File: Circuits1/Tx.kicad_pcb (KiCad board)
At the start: 2 copper layers, 43.2 x 51.4 mm, 54 parts, among them CON1 USB-MINI-B, P1 CONN_3X2, SW1 SW_PUSH, SW2 Power Select, U1 ATMEGA32U4, U2 LD1117, U3 NRF24L01+, U4 MPU-6050, X1 QUARTZ, X2 QUARTZ

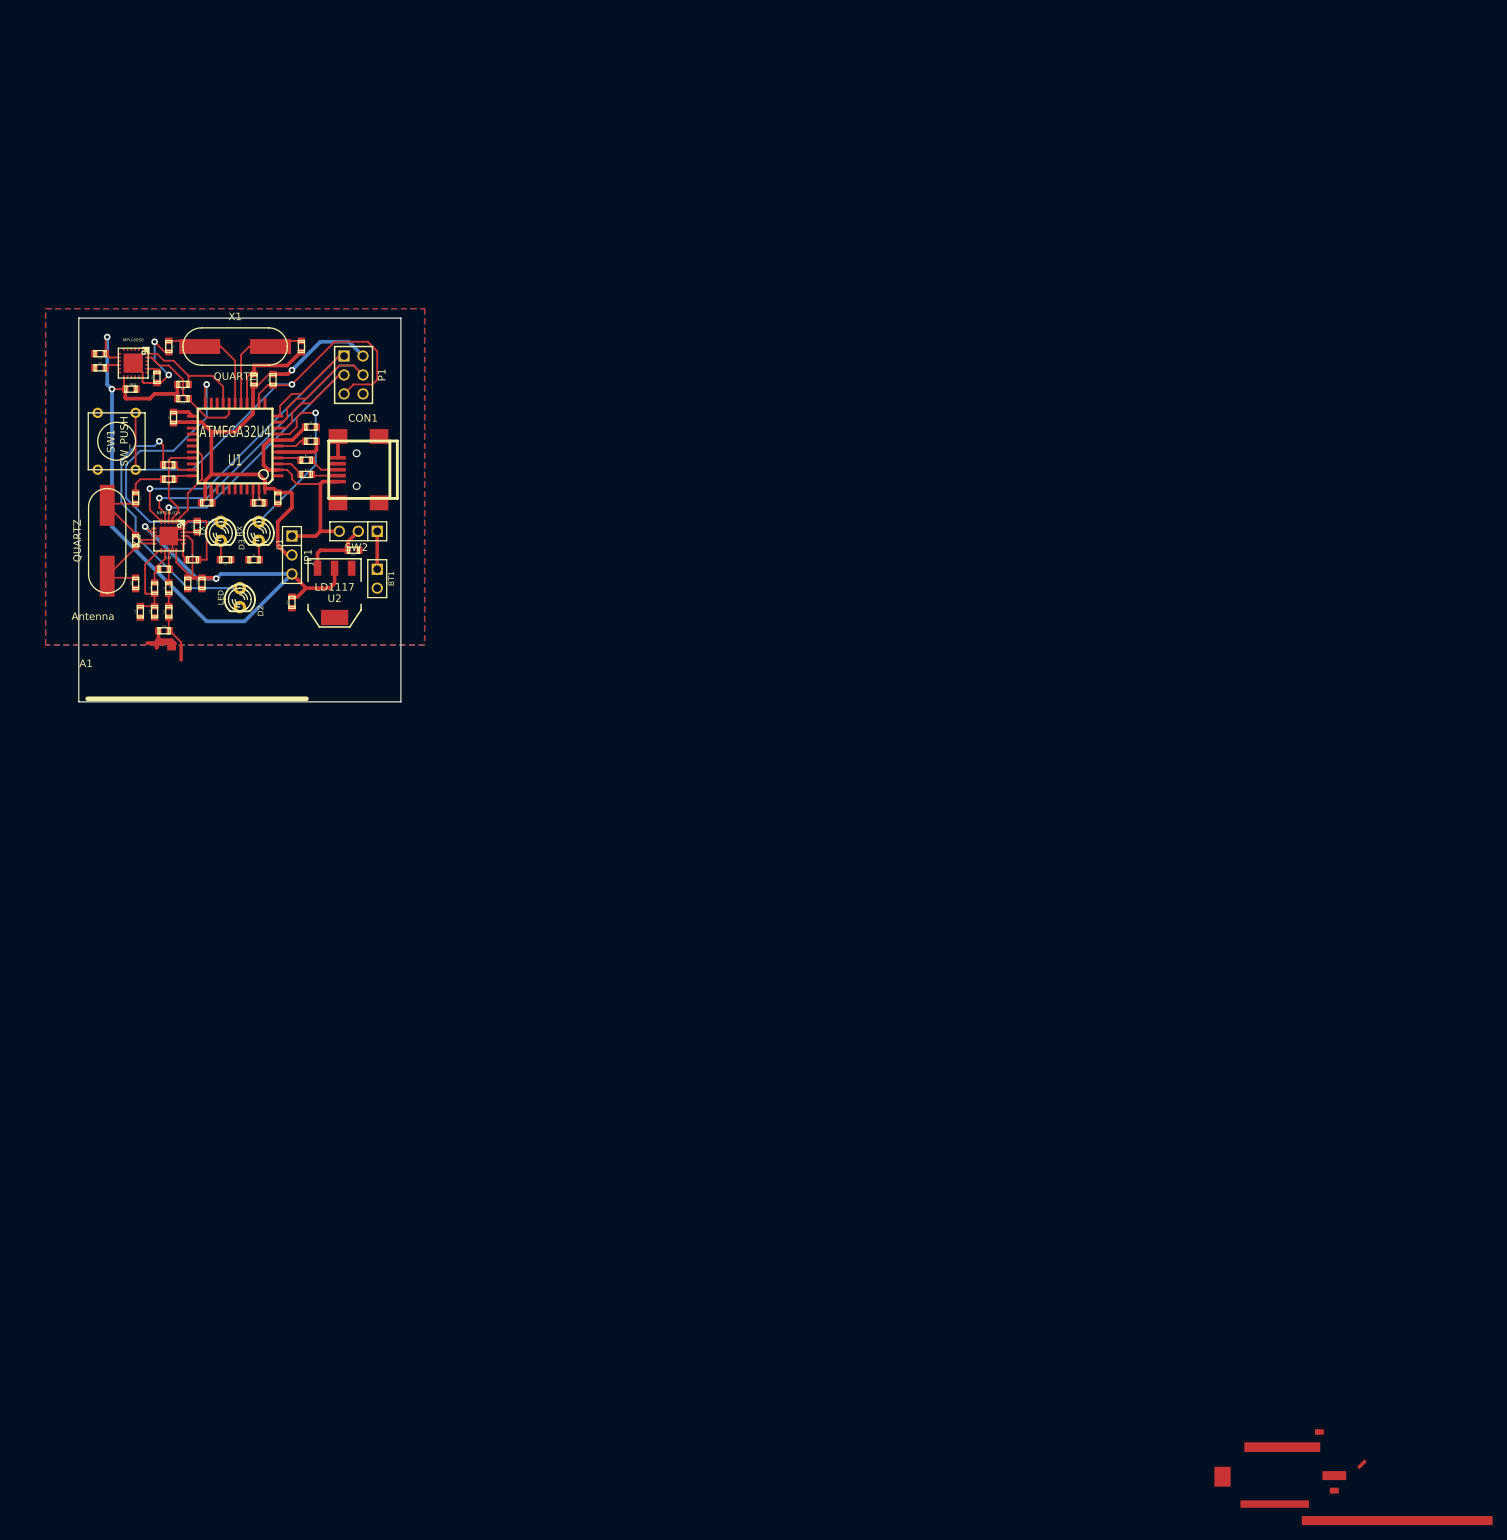
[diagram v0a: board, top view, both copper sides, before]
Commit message: Antenna Position
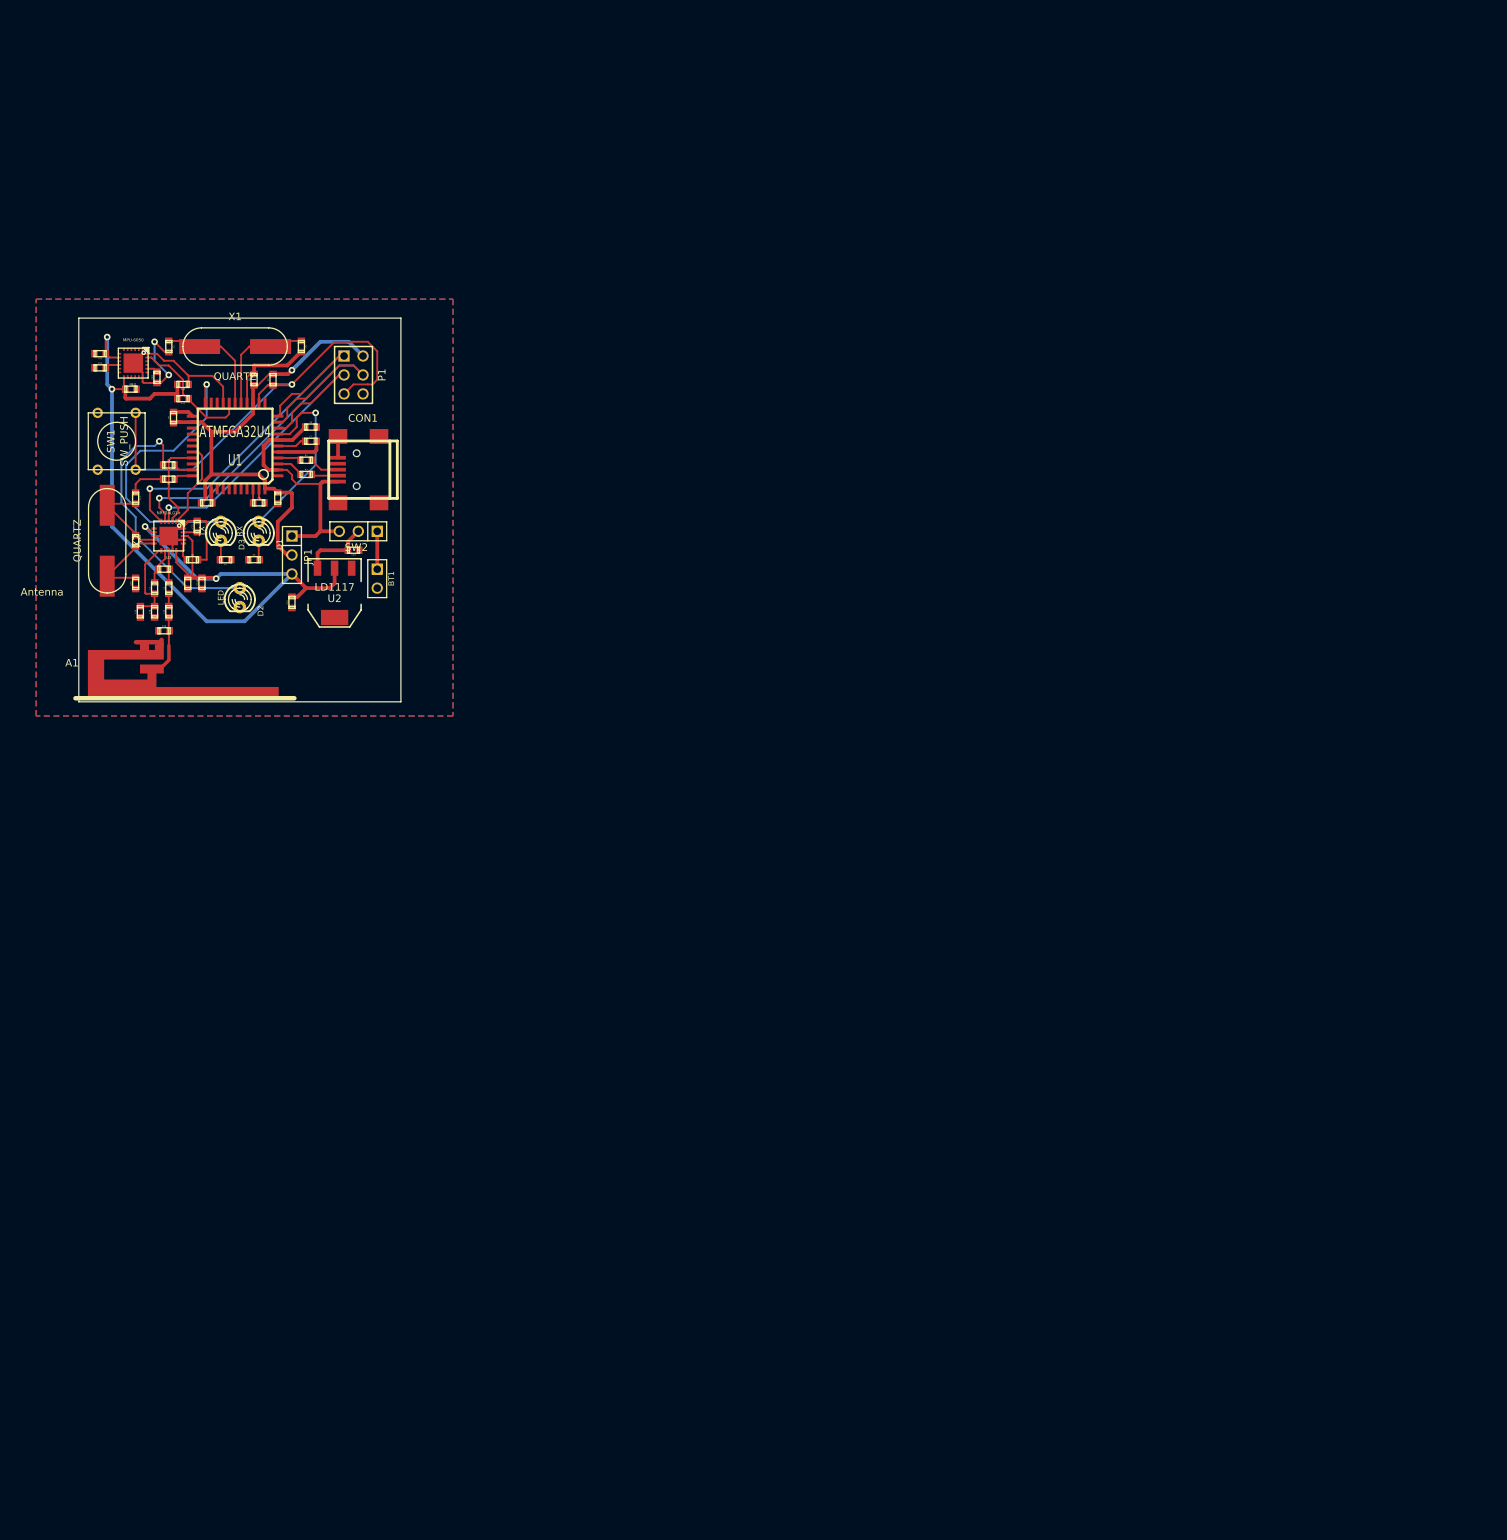
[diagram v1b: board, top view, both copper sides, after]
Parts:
- moved A1 1.89 mm to (157.5, 104.7)
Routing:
- net GND: track 93.6 -> 91.9 mm
- net ANTENNA: track 5.47 -> 4.81 mm
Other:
- net class Power: trace_width 0.5 -> 0.6
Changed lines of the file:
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@@
     (links 133)
     (no_connects 0)
-    (area 145.666884 59.941 189.983533 163.583302)
+    (area 145.364999 60.909999 188.645001 112.445001)
     (thickness 1.6)
     (drawings 4)
-    (tracks 414)
+    (tracks 415)
     (zones 0)
     (modules 54)
@@
     (mod_text_size 1 1)
     (mod_text_width 0.15)
-    (pad_size 25.58 1.21)
+    (pad_size 1.2 0.74)
     (pad_drill 0)
     (pad_to_mask_clearance 0)
@@
   (net_class Power ""
     (clearance 0.254)
-    (trace_width 0.5)
+    (trace_width 0.6)
     (via_dia 0.889)
     (via_drill 0.635)
@@
     (uvia_dia 0.508)
     (uvia_drill 0.127)
-  )
-  (module Antenna (layer F.Cu)
-    (at 159.385 104.775 180)
-    (fp_text reference A1 (at 13 -2.5 180) (layer F.SilkS)
-      (effects (font (size 1 1) (thickness 0.15)))
-    )
-    (fp_text value Antenna (at 12.065 3.81 180) (layer F.SilkS)
-      (effects (font (size 1 1) (thickness 0.15)))
-    )
-    (fp_line (start -16.56 -7.205) (end 12.78 -7.205) (layer F.SilkS) (width 0.61))
-    (pad "" np_thru_hole rect (at -154.325 -111.345) (size 3.2 1.21)
-      (layers *.Mask F.Cu F.SilkS)
-    )
-    (pad "" np_thru_hole rect (at -154.325 -113.355) (size 1.2 0.8)
-      (layers *.Mask F.Cu F.SilkS)
-    )
-    (pad "" np_thru_hole rect (at -162.745 -117.365) (size 25.58 1.21)
-      (layers *.Mask F.Cu F.SilkS)
-    )
-    (pad "" np_thru_hole rect (at -146.345 -115.155) (size 9.18 1)
-      (layers *.Mask F.Cu F.SilkS)
-    )
-    (pad "" np_thru_hole rect (at -139.345 -111.485) (size 2.18 2.67)
-      (layers *.Mask F.Cu F.SilkS)
-    )
-    (pad "" np_thru_hole rect (at -147.345 -107.525) (size 10.18 1.29)
-      (layers *.Mask F.Cu F.SilkS)
-    )
-    (pad 2 smd rect (at 1.53 -0.36) (size 1.2 0.74)
-      (layers F.Cu F.Paste F.Mask)
-      (net 11 GND)
-    )
-    (pad 2 smd rect (at -152.325 -105.495) (size 1.2 0.74)
-      (layers F.Cu F.Paste F.Mask)
-      (net 11 GND)
-    )
-    (pad "" np_thru_hole rect (at -158.03 -109.825 315) (size 0.46 1.4)
-      (layers *.Mask F.Cu F.SilkS)
-    )
-    (pad 1 smd rect (at 0.25 -1.09) (size 0.46 2.2)
-      (layers F.Cu F.Paste F.Mask)
-      (net 10 ANTENNA)
-    )
   )
   (module USB_MINI_B (layer F.Cu)
@@
       (scale (xyz 1 1 1))
       (rotate (xyz 0 0 0))
+    )
+  )
+  (module Antenna (layer F.Cu)
+    (at 157.5 104.69 180)
+    (fp_text reference A1 (at 13 -2.5 180) (layer F.SilkS)
+      (effects (font (size 1 1) (thickness 0.15)))
+    )
+    (fp_text value Antenna (at 17 7 180) (layer F.SilkS)
+      (effects (font (size 1 1) (thickness 0.15)))
+    )
+    (fp_line (start -16.81 -7.225) (end 12.53 -7.225) (layer F.SilkS) (width 0.61))
+    (pad "" np_thru_hole rect (at 2.28 -3.305) (size 3.2 1.21)
+      (layers *.Mask F.Cu F.SilkS)
+    )
+    (pad "" np_thru_hole rect (at 2.28 -4.31) (size 1.2 0.8)
+      (layers *.Mask F.Cu F.SilkS)
+    )
+    (pad "" np_thru_hole rect (at -1.93 -6.315) (size 25.58 1.21)
+      (layers *.Mask F.Cu F.SilkS)
+    )
+    (pad "" np_thru_hole rect (at 6.27 -5.21) (size 9.18 1)
+      (layers *.Mask F.Cu F.SilkS)
+    )
+    (pad "" np_thru_hole rect (at 9.77 -3.375) (size 2.18 2.67)
+      (layers *.Mask F.Cu F.SilkS)
+    )
+    (pad "" np_thru_hole rect (at 5.77 -1.395) (size 10.18 1.29)
+      (layers *.Mask F.Cu F.SilkS)
+    )
+    (pad 2 smd rect (at 1.28 -0.38) (size 1.2 0.74)
+      (layers F.Cu F.Paste F.Mask)
+      (net 11 GND)
+    )
+    (pad 2 smd rect (at 3.28 -0.38) (size 1.2 0.74)
+      (layers F.Cu F.Paste F.Mask)
+      (net 11 GND)
+    )
+    (pad "" np_thru_hole rect (at 0.4275 -2.545 315) (size 0.46 1.4)
+      (layers *.Mask F.Cu F.SilkS)
+    )
+    (pad 1 smd rect (at 0 -1.11) (size 0.46 2.2)
+      (layers F.Cu F.Paste F.Mask)
+      (net 10 ANTENNA)
     )
   )
@@
   (segment (start 160.655 95.76816) (end 160.02 95.76816) (width 0.5) (layer F.Cu) (net 9))
   (segment (start 151.4675 70.70566) (end 151.56434 70.8025) (width 0.254) (layer F.Cu) (net 9))
-  (segment (start 159.135 105.865) (end 159.135 104.40816) (width 0.277) (layer F.Cu) (net 10))
-  (segment (start 159.135 104.40816) (end 157.59684 102.87) (width 0.277) (layer F.Cu) (net 10))
+  (segment (start 157.5 105.8) (end 157.5 102.96684) (width 0.277) (layer F.Cu) (net 10))
+  (segment (start 157.5 102.96684) (end 157.59684 102.87) (width 0.277) (layer F.Cu) (net 10))
   (segment (start 157.48 101.08184) (end 157.48 102.75316) (width 0.254) (layer F.Cu) (net 10))
   (segment (start 157.48 102.75316) (end 157.59684 102.87) (width 0.254) (layer F.Cu) (net 10))
+  (segment (start 156.22 105.07) (end 156.22 105) (width 0.6) (layer F.Cu) (net 11))
+  (segment (start 156.22 105) (end 156.52 104.7) (width 0.6) (layer F.Cu) (net 11))
+  (segment (start 156.52 104.7) (end 156.52 104.09) (width 0.6) (layer F.Cu) (net 11))
+  (segment (start 154.61 104.4) (end 153.08 104.4) (width 0.6) (layer F.Cu) (net 11))
+  (segment (start 156.22 104.4) (end 154.61 104.4) (width 0.6) (layer F.Cu) (net 11))
+  (segment (start 154.22 104.79) (end 154.22 105.07) (width 0.6) (layer F.Cu) (net 11))
+  (segment (start 154.61 104.4) (end 154.22 104.79) (width 0.6) (layer F.Cu) (net 11))
+  (segment (start 156.22 105.07) (end 156.22 104.4) (width 0.6) (layer F.Cu) (net 11))
+  (segment (start 156.22 104.4) (end 156.22 104.36) (width 0.6) (layer F.Cu) (net 11))
+  (segment (start 154.22 105.07) (end 154.22 104.4) (width 0.6) (layer F.Cu) (net 11))
+  (segment (start 154.22 105.07) (end 154.22 105) (width 0.6) (layer F.Cu) (net 11))
+  (segment (start 153.92 104.7) (end 154.22 105.07) (width 0.6) (layer F.Cu) (net 11))
+  (segment (start 154.22 105) (end 153.92 104.7) (width 0.6) (layer F.Cu) (net 11))
+  (segment (start 156.22 105.07) (end 156.22 105) (width 0.6) (layer F.Cu) (net 11))
+  (segment (start 156.22 105.07) (end 156.22 105) (width 0.6) (layer F.Cu) (net 11))
+  (segment (start 156.52 104.7) (end 156.22 105.07) (width 0.6) (layer F.Cu) (net 11))
+  (segment (start 156.22 105) (end 156.52 104.7) (width 0.6) (layer F.Cu) (net 11))
   (segment (start 172.085 78.9051) (end 176.9999 78.9051) (width 0.5) (layer F.Cu) (net 11))
   (segment (start 177.28184 78.62316) (end 177.28184 77.47) (width 0.5) (layer F.Cu) (net 11))
@@
   (segment (start 160.13684 88.14816) (end 161.29 88.14816) (width 0.254) (layer F.Cu) (net 11))
   (segment (start 159.44596 88.83904) (end 160.13684 88.14816) (width 0.254) (layer F.Cu) (net 11))
-  (segment (start 158.242 104.521) (end 157.861 104.14) (width 0.5) (layer F.Cu) (net 11))
-  (segment (start 156.337 104.14) (end 155.855 104.622) (width 0.5) (layer F.Cu) (net 11))
-  (segment (start 157.861 104.14) (end 156.337 104.14) (width 0.5) (layer F.Cu) (net 11))
-  (segment (start 155.855 105.135) (end 155.855 104.622) (width 0.5) (layer F.Cu) (net 11))
-  (segment (start 155.855 104.622) (end 155.855 104.241) (width 0.5) (layer F.Cu) (net 11))
-  (segment (start 155.855 104.241) (end 156.09316 104.00284) (width 0.5) (layer F.Cu) (net 11))
-  (segment (start 156.09316 104.00284) (end 156.09316 102.87) (width 0.5) (layer F.Cu) (net 11))
-  (segment (start 158.242 104.521) (end 158.242 104.748) (width 0.5) (layer F.Cu) (net 11))
-  (segment (start 158.242 104.748) (end 157.855 105.135) (width 0.5) (layer F.Cu) (net 11))
-  (segment (start 155.855 104.648) (end 156.083 104.648) (width 0.5) (layer F.Cu) (net 11))
-  (segment (start 156.21 104.521) (end 158.242 104.521) (width 0.5) (layer F.Cu) (net 11))
-  (segment (start 156.083 104.648) (end 156.21 104.521) (width 0.5) (layer F.Cu) (net 11))
-  (segment (start 155.855 105.135) (end 155.855 104.648) (width 0.5) (layer F.Cu) (net 11))
-  (segment (start 155.855 104.648) (end 155.855 104.547) (width 0.5) (layer F.Cu) (net 11))
-  (segment (start 155.829 104.521) (end 154.559 104.521) (width 0.5) (layer F.Cu) (net 11))
-  (segment (start 155.855 104.547) (end 155.829 104.521) (width 0.5) (layer F.Cu) (net 11))
   (segment (start 169.5704 83.82) (end 169.5704 84.99856) (width 0.254) (layer F.Cu) (net 11))
   (segment (start 169.5704 84.99856) (end 170.29684 85.725) (width 0.254) (layer F.Cu) (net 11))
@@
     (polygon
       (pts
-        (xy 191.77 116.205) (xy 140.97 116.205) (xy 140.97 104.775) (xy 191.77 104.775)
+        (xy 153.6 104.7) (xy 143.2 104.7) (xy 143.2 113.7) (xy 192.8 113.7) (xy 192.8 104.7)
+        (xy 153.6 104.7)
+      )
+    )
+  )
+  (zone (net 0) (net_name "") (layer B.Cu) (hatch edge 0.508)
+    (connect_pads (clearance 0.508))
+    (min_thickness 0.254)
+    (keepout (tracks allowed) (vias allowed) (copperpour not_allowed))
+    (fill (arc_segments 16) (thermal_gap 0.508) (thermal_bridge_width 0.508))
+    (polygon
+      (pts
+        (xy 153.6 104.7) (xy 143.2 104.7) (xy 143.2 113.7) (xy 192.8 113.7) (xy 192.8 104.7)
+        (xy 153.6 104.7)
       )
     )
@@
     (connect_pads (clearance 0.508))
     (min_thickness 0.254)
-    (fill (arc_segments 16) (thermal_gap 0.508) (thermal_bridge_width 0.508) (smoothing fillet))
+    (fill (arc_segments 16) (thermal_gap 0.508) (thermal_bridge_width 0.508))
     (polygon
       (pts
-        (xy 191.77 104.775) (xy 140.97 104.775) (xy 140.97 59.69) (xy 191.77 59.69)
+        (xy 195.58 114.3) (xy 139.7 114.3) (xy 139.7 58.42) (xy 195.58 58.42)
       )
     )
@@
     (connect_pads (clearance 0.508))
     (min_thickness 0.254)
-    (fill (arc_segments 16) (thermal_gap 0.508) (thermal_bridge_width 0.508) (smoothing fillet))
+    (fill (arc_segments 16) (thermal_gap 0.508) (thermal_bridge_width 0.508))
     (polygon
       (pts
-        (xy 191.77 104.775) (xy 140.97 104.775) (xy 140.97 59.69) (xy 191.77 59.69)
+        (xy 195.58 114.3) (xy 139.7 114.3) (xy 139.7 58.42) (xy 195.58 58.42)
       )
     )

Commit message: PDFs
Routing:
- net 3V3: track 126.3 -> 161.2 mm
- net GND: track 91.9 -> 100.3 mm
- net N-000008: track 37.3 -> 39.6 mm
- net N-000007: track 24.8 -> 26.6 mm
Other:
- net class Ant: trace_width 0.277 -> 0.27686
- net class Power: trace_width 0.6 -> 0.59944

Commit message: Neatened Schematics and Final PCB
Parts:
- added Hole1: CONN_1, Drill3mm, F.Cu at (151.4, 51.6)
- added Hole2: CONN_1, Drill3mm, F.Cu at (174.9, 51.6)
- R5, R6, R7: moved to B.Cu
- moved D2 61.9 mm to (151.1, 38.6)
- moved SW1 54.5 mm to (176.3, 29.5), turned to 180 degrees
- moved R5 50.2 mm to (146.8, 48.3), turned to 90 degrees
- moved R7 49.3 mm to (145.0, 48.3), turned to 90 degrees
- moved D1 48.8 mm to (151.4, 44.2)
- moved D3 48.7 mm to (146.6, 44.2)
- moved BT1 46.6 mm to (180.8, 49.5), turned to 90 degrees
- moved R6 42.6 mm to (148.1, 39.1), turned to 270 degrees
- moved C5 41.4 mm to (165.9, 27.9), turned to 0 degrees
- moved CON1 41.3 mm to (178.3, 40.3)
- moved R3 41.0 mm to (171.4, 41.1)
- moved U2 40.9 mm to (167.6, 58.7), turned to 0 degrees
- moved R2 40.9 mm to (171.4, 39.4)
- moved U1 40.8 mm to (162.4, 37.5)
- moved R11 40.7 mm to (153.7, 31.5), turned to 270 degrees
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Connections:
- U4 pad 9: (no net) -> GND
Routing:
- net GND: track 100.3 -> 168.6 mm, vias 2 -> 15
- net 3V3: track 161.2 -> 112.7 mm, vias 4 -> 5
- net N-000002: track 39.6 -> 3.47 mm, vias 1 -> 0
- net VCC: track 72.2 -> 93.4 mm
- net N-0000012: track 26.6 -> 46.6 mm
- net N-000009: track 38.9 -> 23.4 mm
- net /ICSP Header/SCK: track 45.3 -> 59.7 mm, vias 1 -> 2
- net /Radio/CE: track 11.7 -> 25.3 mm, vias 0 -> 2
- net /ICSP Header/MISO: track 51.3 -> 63.3 mm, vias 1 -> 2
- net /Radio/CSN: track 12.3 -> 21.9 mm, vias 0 -> 2
- net N-000001: track 2.70 -> 10.1 mm, vias 0 -> 1
- net N-000008: track 16.8 -> 23.6 mm
- net N-0000052: track 12.1 -> 18.3 mm
- net RESET: track 62.9 -> 68.4 mm
- net /ICSP Header/MOSI: track 54.5 -> 58.7 mm, vias 1 -> 2
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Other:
- board size 43.2 x 51.4 mm -> 38 x 54 mm
- net class Ant: via_dia 0.889 -> 1.2; via_drill 0.635 -> 0.8
- net class Default: via_dia 0.889 -> 1.2; via_drill 0.635 -> 0.8
- net class FAT added: clearance 0.254, trace_width 1.2, via_dia 1.2, via_drill 0.8
- net class Power: via_dia 0.889 -> 1.2; via_drill 0.635 -> 0.8
- net class Power (thin): via_dia 0.889 -> 1.2; via_drill 0.635 -> 0.8
- board text added: "Jon Elmer 2014"
